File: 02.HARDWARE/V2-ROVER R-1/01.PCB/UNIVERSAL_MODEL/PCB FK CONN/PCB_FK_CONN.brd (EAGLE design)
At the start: 22.9 x 23.3 mm, 0 parts

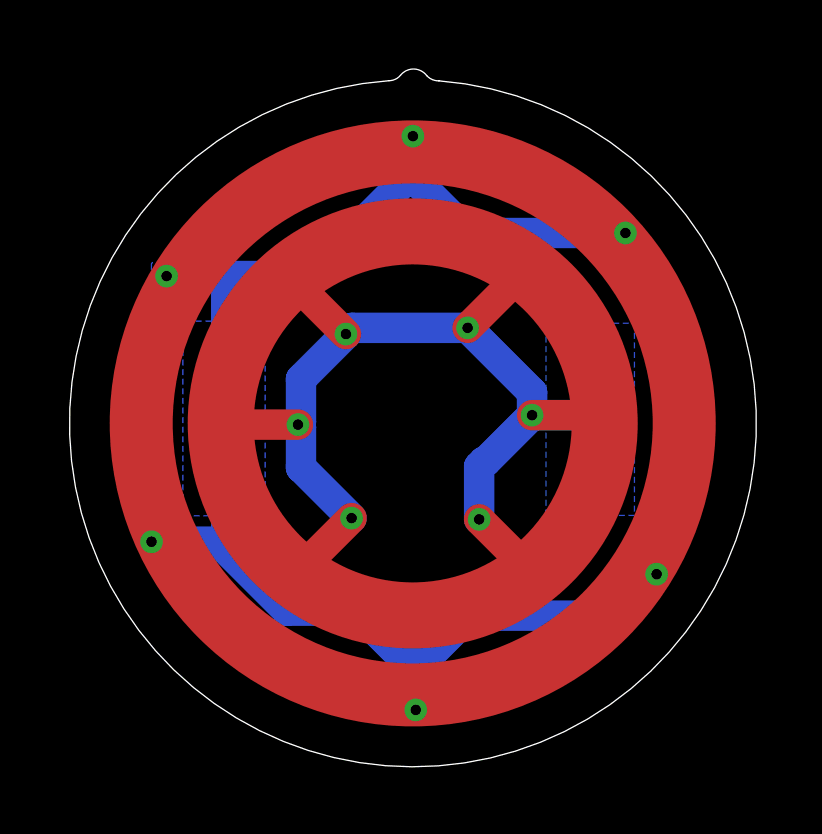
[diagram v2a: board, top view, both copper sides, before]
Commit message: Se modifica el tamaño para adaptar a la mecanica mejor (mas pequeño)
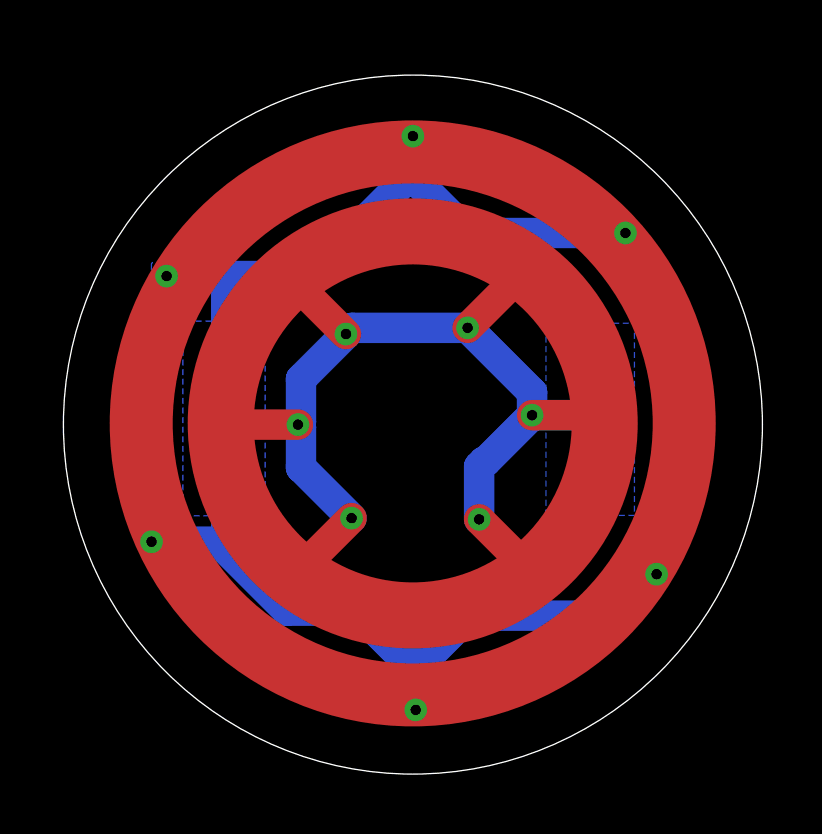
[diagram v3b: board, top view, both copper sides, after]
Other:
- board size 22.9 x 23.3 mm -> 23.3 x 23.3 mm
- board text added: "FK_CONN v3-Sep'24"
- board text added: "NEGRO"
- board text added: "ROJO"
- board text removed: "EXT"
- board text removed: "FK_CONN v2-Jul'24"
- board text removed: "INT"
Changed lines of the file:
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@@
 <grid distance="0.01" unitdist="mm" unit="mm" style="lines" multiple="1" display="yes" altdistance="5" altunitdist="mil" altunit="mil"/>
 <layers>
-<layer number="1" name="Top" color="4" fill="1" visible="no" active="yes"/>
+<layer number="1" name="Top" color="4" fill="1" visible="yes" active="yes"/>
 <layer number="16" name="Bottom" color="1" fill="1" visible="yes" active="yes"/>
 <layer number="17" name="Pads" color="2" fill="1" visible="yes" active="yes"/>
@@
 <layer number="19" name="Unrouted" color="6" fill="1" visible="yes" active="yes"/>
 <layer number="20" name="Dimension" color="24" fill="1" visible="yes" active="yes"/>
-<layer number="21" name="tPlace" color="7" fill="1" visible="no" active="yes"/>
+<layer number="21" name="tPlace" color="7" fill="1" visible="yes" active="yes"/>
 <layer number="22" name="bPlace" color="7" fill="1" visible="yes" active="yes"/>
-<layer number="23" name="tOrigins" color="15" fill="1" visible="no" active="yes"/>
+<layer number="23" name="tOrigins" color="15" fill="1" visible="yes" active="yes"/>
 <layer number="24" name="bOrigins" color="15" fill="1" visible="yes" active="yes"/>
-<layer number="25" name="tNames" color="7" fill="1" visible="no" active="yes"/>
+<layer number="25" name="tNames" color="7" fill="1" visible="yes" active="yes"/>
 <layer number="26" name="bNames" color="7" fill="1" visible="yes" active="yes"/>
 <layer number="27" name="tValues" color="7" fill="1" visible="no" active="yes"/>
@@
 <layer number="37" name="tTest" color="7" fill="1" visible="no" active="yes"/>
 <layer number="38" name="bTest" color="7" fill="1" visible="no" active="yes"/>
-<layer number="39" name="tKeepout" color="4" fill="11" visible="no" active="yes"/>
+<layer number="39" name="tKeepout" color="4" fill="11" visible="yes" active="yes"/>
 <layer number="40" name="bKeepout" color="1" fill="11" visible="yes" active="yes"/>
-<layer number="41" name="tRestrict" color="4" fill="10" visible="no" active="yes"/>
+<layer number="41" name="tRestrict" color="4" fill="10" visible="yes" active="yes"/>
 <layer number="42" name="bRestrict" color="1" fill="10" visible="yes" active="yes"/>
 <layer number="43" name="vRestrict" color="2" fill="10" visible="no" active="yes"/>
@@
 <layer number="49" name="Reference" color="7" fill="1" visible="no" active="yes"/>
 <layer number="50" name="dxf" color="7" fill="1" visible="no" active="no"/>
-<layer number="51" name="tDocu" color="7" fill="1" visible="no" active="yes"/>
+<layer number="51" name="tDocu" color="7" fill="1" visible="yes" active="yes"/>
 <layer number="52" name="bDocu" color="7" fill="1" visible="yes" active="yes"/>
 <layer number="53" name="tGND_GNDA" color="7" fill="9" visible="no" active="no"/>
@@
 <board>
 <plain>
-<wire x1="72.466109375" y1="82.59346875" x2="72.873509375" y2="82.41830625" width="0.001" layer="20" curve="48.464246"/>
-<wire x1="71.210490625" y1="82.423309375" x2="71.589890625" y2="82.599471875" width="0.001" layer="20" curve="48.46403"/>
-<wire x1="72.466109375" y1="82.59346875" x2="71.589890625" y2="82.599471875" width="0.001" layer="20" curve="105.105949"/>
 <circle x="72" y="71" radius="6.4" width="2.2" layer="29"/>
-<wire x1="71.210490625" y1="82.423309375" x2="72.873509375" y2="82.41830625" width="0.001" layer="20" curve="351.67"/>
 <circle x="72" y="71" radius="9.05" width="2.1" layer="29"/>
-<circle x="72" y="71" radius="10.1" width="0.001" layer="48"/>
+<circle x="72" y="71" radius="10.75" width="0.001" layer="48"/>
 <circle x="72" y="71" radius="7.5" width="0.001" layer="48"/>
 <circle x="72" y="71" radius="5.3" width="0.001" layer="29"/>
@@
 <vertex x="67.161" y="67.911"/>
 </polygon>
-<text x="67.7" y="74.9" size="1.778" layer="22" font="vector" rot="MR0">EXT</text>
-<text x="79.6" y="74.8" size="1.778" layer="22" font="vector" rot="MR0">INT</text>
+<text x="67.71" y="74.67" size="1.016" layer="22" font="vector" rot="MR0">NEGRO</text>
+<text x="79.6" y="74.67" size="1.016" layer="22" font="vector" rot="MR0">ROJO</text>
 <text x="75" y="63.46" size="1.016" layer="22" font="vector" rot="MR0">FK_CONN
-v2-Jul'24</text>
+v3-Sep'24</text>
 <text x="75.8" y="68.45" size="1.016" layer="22" font="vector" rot="MR0">"I love it
 when a plan
 comes
 together"</text>
+<circle x="72.00701875" y="70.96" radius="7.5" width="0.001" layer="48"/>
+<circle x="72.00701875" y="70.96" radius="5.3" width="0.001" layer="48"/>
+<circle x="72.00701875" y="70.96" radius="10.35" width="0.001" layer="48"/>
+<circle x="72.00701875" y="70.96" radius="11.65" width="0.001" layer="20"/>
+<circle x="72.00701875" y="70.96" radius="8" width="0.001" layer="48"/>
+<circle x="72.05" y="71.03" radius="10.1" width="0.001" layer="48"/>
 </plain>
 <attributes>
@@
 <mfgpreviewcolor name="substratecolor" color="0xFF786E46"/>
 </mfgpreviewcolors>
+<errors>
+</errors>
 </board>
 </drawing>
